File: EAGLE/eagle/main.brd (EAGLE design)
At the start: 78.4 x 61 mm, 29 parts, among them IC1 317T, IC2 ATMEGA168-20P, IC3 25LC080P, IC4 ESP-WROOM-02FRONT-FACE, IC5 AT42QT1070-SSU, Q1 FQN1N50CI, Q2 FQN1N50CI, Q3 FQN1N50CI

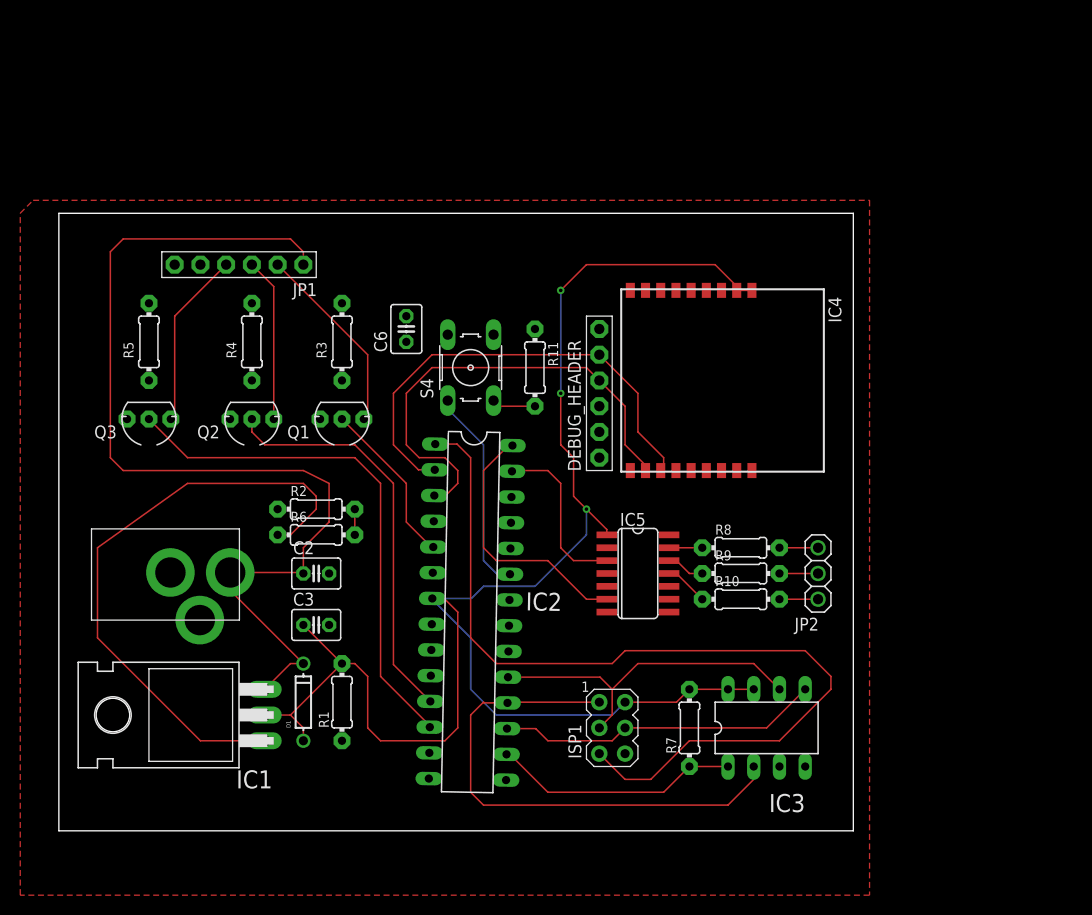
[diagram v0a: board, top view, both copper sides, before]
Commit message: changed schematic
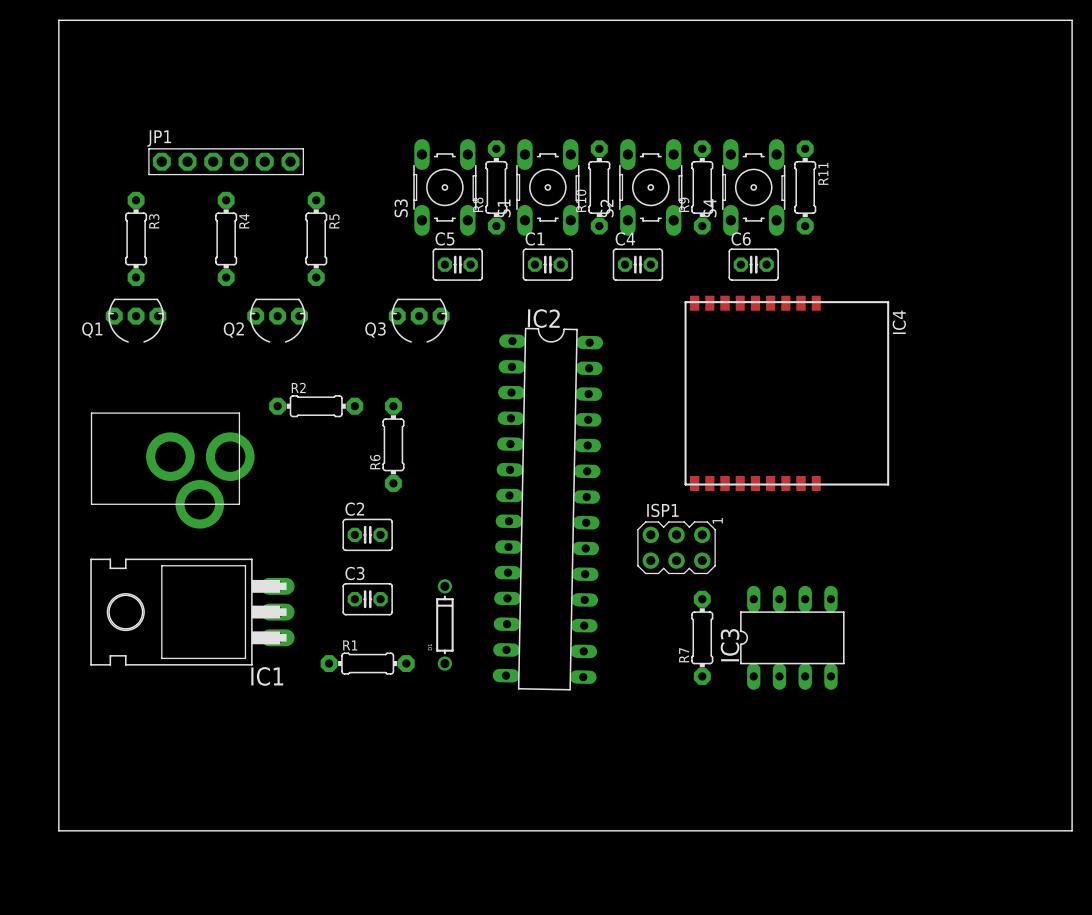
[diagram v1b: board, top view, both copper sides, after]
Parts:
- removed DEBUG_HEADER: (no value), adafruit:1X06-BIG
- removed IC5: AT42QT1070-SSU, adafruit:SO14
- removed JP2: (no value), adafruit:1X03
- added C1, C4, C5: 0.1uF, adafruit:C025-030X050
- added S1, S2, S3: (no value), switch-omron:B3F-10XX
- R10, R8, R9: value 10K -> 1K
- moved R10 43.0 mm to (53.3, 63.5), turned to 90 degrees
- moved R8 43.0 mm to (43.2, 63.5), turned to 90 degrees
- moved R9 38.3 mm to (63.5, 63.5), turned to 90 degrees
- moved C6 34.9 mm to (68.6, 55.9), turned to 0 degrees
- moved S4 33.1 mm to (68.6, 63.5)
- moved R11 32.1 mm to (73.7, 63.5)
- moved Q3 28.5 mm to (35.6, 50.8)
- moved R3 22.7 mm to (7.62, 58.4)
- moved Q1 22.7 mm to (7.62, 50.8)
- moved R5 19.4 mm to (25.4, 58.4)
- moved ISP1 18.9 mm to (61.0, 27.9), turned to 270 degrees
- moved D1 15.9 mm to (38.1, 20.3)
- moved IC2 12.7 mm to (48.3, 31.8)
- moved R6 11.7 mm to (33.0, 38.1), turned to 90 degrees
- moved U$1 11.4 mm to (7.62, 36.8)
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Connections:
- removed net CHANGE: IC5.5
- removed net KEY_0: JP2.3, R8.2
- removed net KEY_1: JP2.2, R9.2
- removed net KEY_2: JP2.1, R10.2
- removed net SCL: IC2.28, IC5.6
- removed net SDA: IC2.27, IC5.3
- new net N$10: R10.1, S1.3
- new net N$7: R8.1, S3.3
- new net N$9: R9.1, S2.3
- net GND: now also C1.2, C4.2, C5.2, R10.2, R8.2, R9.2; no longer DEBUG_HEADER.1, IC5.14, IC5.2
- net MAS_RX: no longer DEBUG_HEADER.5
- net MAS_TX: no longer DEBUG_HEADER.4
- net N$1: now also C1.1, IC2.24, S3.1; no longer IC5.13, R8.1
- net N$2: now also C4.1, IC2.25, S2.1; no longer IC5.12, R9.1
- net N$3: now also C5.1, IC2.26, S1.1; no longer IC5.11, R10.1
- net VCC: no longer IC5.1
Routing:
- net VCC: track 158.7 -> 0.00 mm, vias 3 -> 0
- net VIN: track 98.2 -> 0.00 mm
- net RST: track 89.8 -> 0.00 mm
- net N$6: track 59.9 -> 0.00 mm
- net MISO: track 51.7 -> 0.00 mm
- net N$5: track 51.6 -> 0.00 mm
- net MAS_TX: track 46.7 -> 0.00 mm
- net MAS_RX: track 46.3 -> 0.00 mm
- net N$16: track 40.4 -> 0.00 mm
- net SCK: track 33.7 -> 0.00 mm
- net MOSI: track 32.0 -> 0.00 mm
- net SCL: track 25.8 -> 0.00 mm
- net SS: track 24.6 -> 0.00 mm
- net SN_PROG_EN: track 20.4 -> 0.00 mm
- net N$8: track 19.1 -> 0.00 mm
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- removed copper zone on layer 1, net GND
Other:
- board size 78.4 x 61 mm -> 100 x 80 mm
